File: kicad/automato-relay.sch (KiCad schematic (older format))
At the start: 30 parts, among them J1 Screw_Terminal_01x03, J2 Screw_Terminal_01x03, J3 Screw_Terminal_01x03, J4 Screw_Terminal_01x05, J5 Screw_Terminal_01x03, J6 Screw_Terminal_01x03, J7 Screw_Terminal_01x05, J8 Screw_Terminal_01x03, K1 G5LE-14, K2 G5LE-14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

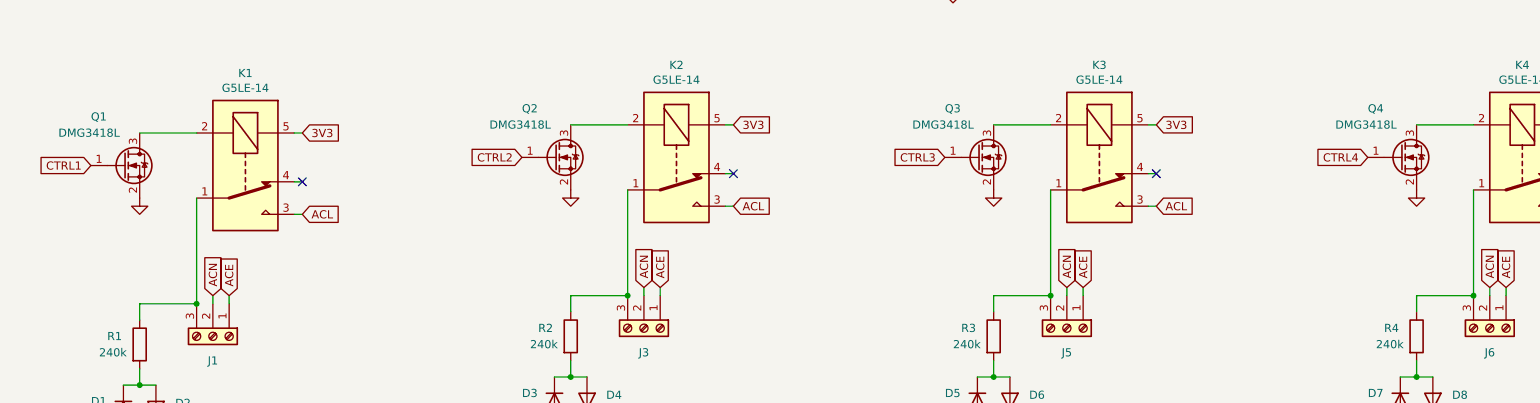
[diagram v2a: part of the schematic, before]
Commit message: add pull-down resistors to MOSFET gates
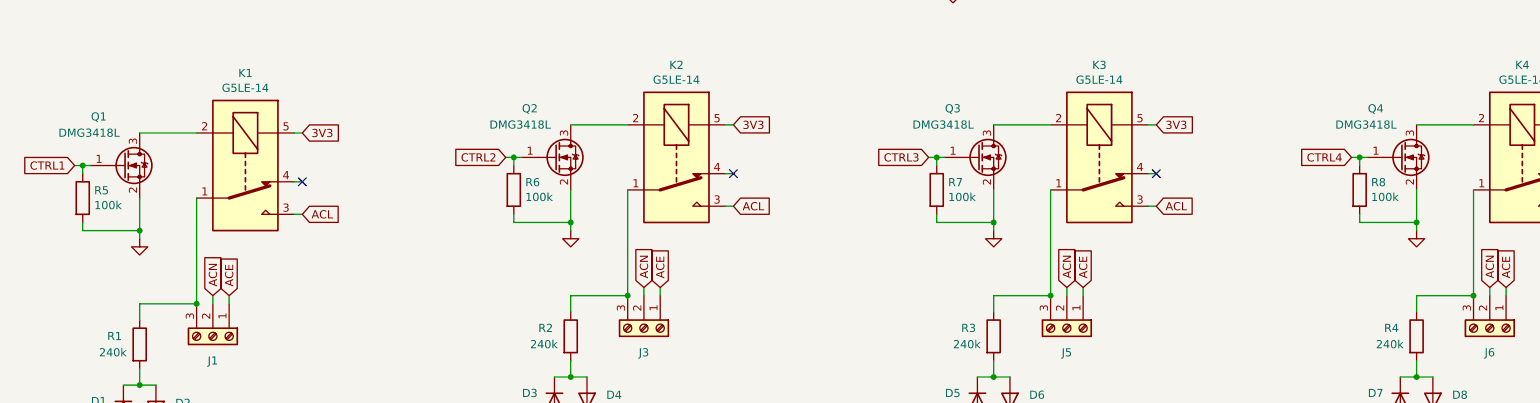
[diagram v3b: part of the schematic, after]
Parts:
- added R5, R6, R7, R8: 100k, symbol Device:R
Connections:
- net CTRL1: now also R5.1
- net CTRL2: now also R6.1
- net CTRL3: now also R7.1
- net CTRL4: now also R8.1
- net GND: now also R5.2, R6.2, R7.2, R8.2
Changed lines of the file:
@@
 L power:GND #PWR02
 U 1 1 60165E6B
-P 1600 4400
-F 0 "#PWR02" H 1600 4150 50  0001 C CNN
-F 1 "GND" H 1450 4350 50  0001 C CNN
-F 2 "" H 1600 4400 50  0001 C CNN
-F 3 "" H 1600 4400 50  0001 C CNN
-	1    1600 4400
+P 1600 4650
+F 0 "#PWR02" H 1600 4400 50  0001 C CNN
+F 1 "GND" H 1450 4600 50  0001 C CNN
+F 2 "" H 1600 4650 50  0001 C CNN
+F 3 "" H 1600 4650 50  0001 C CNN
+	1    1600 4650
 	1    0    0    -1
 $EndComp
@@
 Text GLabel 2600 4500 2    50   Input ~ 0
 ACL
-Text GLabel 1300 4200 0    50   Input ~ 0
+Text GLabel 1200 4200 0    50   Input ~ 0
 CTRL1
 Wire Wire Line
@@
 Text GLabel 5250 4450 2    50   Input ~ 0
 ACL
-Text GLabel 3950 4150 0    50   Input ~ 0
+Text GLabel 3850 4150 0    50   Input ~ 0
 CTRL2
 Wire Wire Line
@@
 Text GLabel 7850 4450 2    50   Input ~ 0
 ACL
-Text GLabel 6550 4150 0    50   Input ~ 0
+Text GLabel 6450 4150 0    50   Input ~ 0
 CTRL3
 Wire Wire Line
@@
 Text GLabel 10450 4450 2    50   Input ~ 0
 ACL
-Text GLabel 9150 4150 0    50   Input ~ 0
+Text GLabel 9050 4150 0    50   Input ~ 0
 CTRL4
 Wire Wire Line
@@
 Text GLabel 9450 5900 3    50   Input ~ 0
 ACN
-$Comp
-L Transistor_FET:DMG3418L Q1
-U 1 1 6025169E
-P 1500 4200
-F 0 "Q1" H 1300 4500 50  0000 L CNN
-F 1 "DMG3418L" H 1100 4400 50  0000 L CNN
-F 2 "Package_TO_SOT_SMD:SOT-23" H 1700 4125 50  0001 L CIN
-F 3 "http://www.diodes.com/assets/Datasheets/DMG3418L.pdf" H 1500 4200 50  0001 L CNN
-	1    1500 4200
-	1    0    0    -1
-$EndComp
 Wire Wire Line
 	1600 4000 1950 4000
 Text GLabel 2600 4000 2    50   Input ~ 0
 3V3
-$Comp
-L power:GND #PWR01
-U 1 1 6025E6F9
-P 4250 4350
-F 0 "#PWR01" H 4250 4100 50  0001 C CNN
-F 1 "GND" H 4100 4300 50  0001 C CNN
-F 2 "" H 4250 4350 50  0001 C CNN
-F 3 "" H 4250 4350 50  0001 C CNN
-	1    4250 4350
-	1    0    0    -1
-$EndComp
 $Comp
 L Transistor_FET:DMG3418L Q2
@@
 	4250 3950 4600 3950
 $Comp
-L power:GND #PWR03
-U 1 1 6026325E
-P 6850 4350
-F 0 "#PWR03" H 6850 4100 50  0001 C CNN
-F 1 "GND" H 6700 4300 50  0001 C CNN
-F 2 "" H 6850 4350 50  0001 C CNN
-F 3 "" H 6850 4350 50  0001 C CNN
-	1    6850 4350
-	1    0    0    -1
-$EndComp
-$Comp
 L Transistor_FET:DMG3418L Q3
 U 1 1 60263271
@@
 Wire Wire Line
 	6850 3950 7200 3950
-$Comp
-L power:GND #PWR04
-U 1 1 602684FF
-P 9450 4350
-F 0 "#PWR04" H 9450 4100 50  0001 C CNN
-F 1 "GND" H 9300 4300 50  0001 C CNN
-F 2 "" H 9450 4350 50  0001 C CNN
-F 3 "" H 9450 4350 50  0001 C CNN
-	1    9450 4350
-	1    0    0    -1
-$EndComp
 $Comp
 L Transistor_FET:DMG3418L Q4
@@
 Wire Wire Line
 	4800 4950 4800 5000
+$Comp
+L Device:R R5
+U 1 1 6030A4D9
+P 1250 4400
+F 0 "R5" H 1320 4446 50  0000 L CNN
+F 1 "100k" H 1320 4355 50  0000 L CNN
+F 2 "" V 1180 4400 50  0001 C CNN
+F 3 "~" H 1250 4400 50  0001 C CNN
+	1    1250 4400
+	1    0    0    -1
+$EndComp
+Wire Wire Line
+	1200 4200 1250 4200
+Wire Wire Line
+	1250 4200 1250 4250
+Connection ~ 1250 4200
+Wire Wire Line
+	1250 4200 1300 4200
+Wire Wire Line
+	1250 4550 1250 4600
+Wire Wire Line
+	1250 4600 1600 4600
+Wire Wire Line
+	1600 4400 1600 4600
+Connection ~ 1600 4600
+$Comp
+L power:GND #PWR01
+U 1 1 6031750C
+P 4250 4600
+F 0 "#PWR01" H 4250 4350 50  0001 C CNN
+F 1 "GND" H 4100 4550 50  0001 C CNN
+F 2 "" H 4250 4600 50  0001 C CNN
+F 3 "" H 4250 4600 50  0001 C CNN
+	1    4250 4600
+	1    0    0    -1
+$EndComp
+$Comp
+L Device:R R6
+U 1 1 6031751E
+P 3900 4350
+F 0 "R6" H 3970 4396 50  0000 L CNN
+F 1 "100k" H 3970 4305 50  0000 L CNN
+F 2 "" V 3830 4350 50  0001 C CNN
+F 3 "~" H 3900 4350 50  0001 C CNN
+	1    3900 4350
+	1    0    0    -1
+$EndComp
+Wire Wire Line
+	3900 4500 3900 4550
+Wire Wire Line
+	3900 4550 4250 4550
+Wire Wire Line
+	4250 4350 4250 4550
+Connection ~ 4250 4550
+Wire Wire Line
+	3850 4150 3900 4150
+Wire Wire Line
+	3900 4150 3900 4200
+Connection ~ 3900 4150
+Wire Wire Line
+	3900 4150 3950 4150
+$Comp
+L Transistor_FET:DMG3418L Q1
+U 1 1 6025169E
+P 1500 4200
+F 0 "Q1" H 1300 4500 50  0000 L CNN
+F 1 "DMG3418L" H 1100 4400 50  0000 L CNN
+F 2 "Package_TO_SOT_SMD:SOT-23" H 1700 4125 50  0001 L CIN
+F 3 "http://www.diodes.com/assets/Datasheets/DMG3418L.pdf" H 1500 4200 50  0001 L CNN
+	1    1500 4200
+	1    0    0    -1
+$EndComp
+Wire Wire Line
+	4250 4550 4250 4600
+Wire Wire Line
+	1600 4600 1600 4650
+$Comp
+L power:GND #PWR03
+U 1 1 60330C2B
+P 6850 4600
+F 0 "#PWR03" H 6850 4350 50  0001 C CNN
+F 1 "GND" H 6700 4550 50  0001 C CNN
+F 2 "" H 6850 4600 50  0001 C CNN
+F 3 "" H 6850 4600 50  0001 C CNN
+	1    6850 4600
+	1    0    0    -1
+$EndComp
+$Comp
+L Device:R R7
+U 1 1 60330C3D
+P 6500 4350
+F 0 "R7" H 6570 4396 50  0000 L CNN
+F 1 "100k" H 6570 4305 50  0000 L CNN
+F 2 "" V 6430 4350 50  0001 C CNN
+F 3 "~" H 6500 4350 50  0001 C CNN
+	1    6500 4350
+	1    0    0    -1
+$EndComp
+Wire Wire Line
+	6500 4500 6500 4550
+Wire Wire Line
+	6500 4550 6850 4550
+Wire Wire Line
+	6850 4350 6850 4550
+Connection ~ 6850 4550
+Wire Wire Line
+	6850 4550 6850 4600
+Wire Wire Line
+	6450 4150 6500 4150
+Wire Wire Line
+	6500 4150 6500 4200
+Connection ~ 6500 4150
+Wire Wire Line
+	6500 4150 6550 4150
+$Comp
+L power:GND #PWR04
+U 1 1 6033C766
+P 9450 4600
+F 0 "#PWR04" H 9450 4350 50  0001 C CNN
+F 1 "GND" H 9300 4550 50  0001 C CNN
+F 2 "" H 9450 4600 50  0001 C CNN
+F 3 "" H 9450 4600 50  0001 C CNN
+	1    9450 4600
+	1    0    0    -1
+$EndComp
+$Comp
+L Device:R R8
+U 1 1 6033C778
+P 9100 4350
+F 0 "R8" H 9170 4396 50  0000 L CNN
+F 1 "100k" H 9170 4305 50  0000 L CNN
+F 2 "" V 9030 4350 50  0001 C CNN
+F 3 "~" H 9100 4350 50  0001 C CNN
+	1    9100 4350
+	1    0    0    -1
+$EndComp
+Wire Wire Line
+	9100 4500 9100 4550
+Wire Wire Line
+	9100 4550 9450 4550
+Wire Wire Line
+	9450 4350 9450 4550
+Connection ~ 9450 4550
+Wire Wire Line
+	9450 4550 9450 4600
+Wire Wire Line
+	9150 4150 9100 4150
+Wire Wire Line
+	9100 4150 9100 4200
+Connection ~ 9100 4150
+Wire Wire Line
+	9100 4150 9050 4150
 $EndSCHEMATC

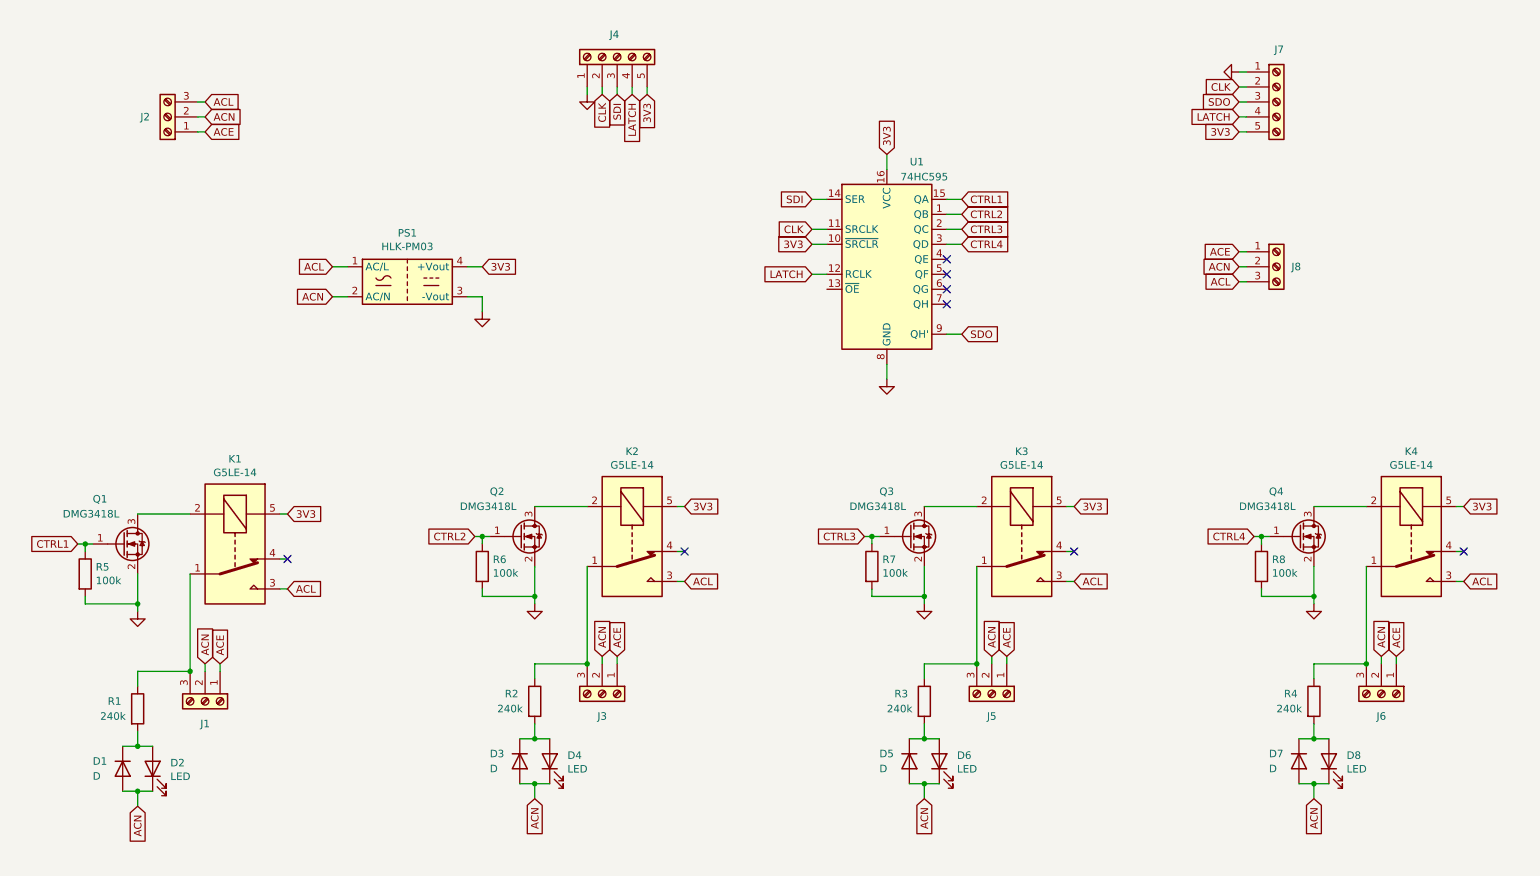
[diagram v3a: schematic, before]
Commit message: add TE-3-213598-4 symbol
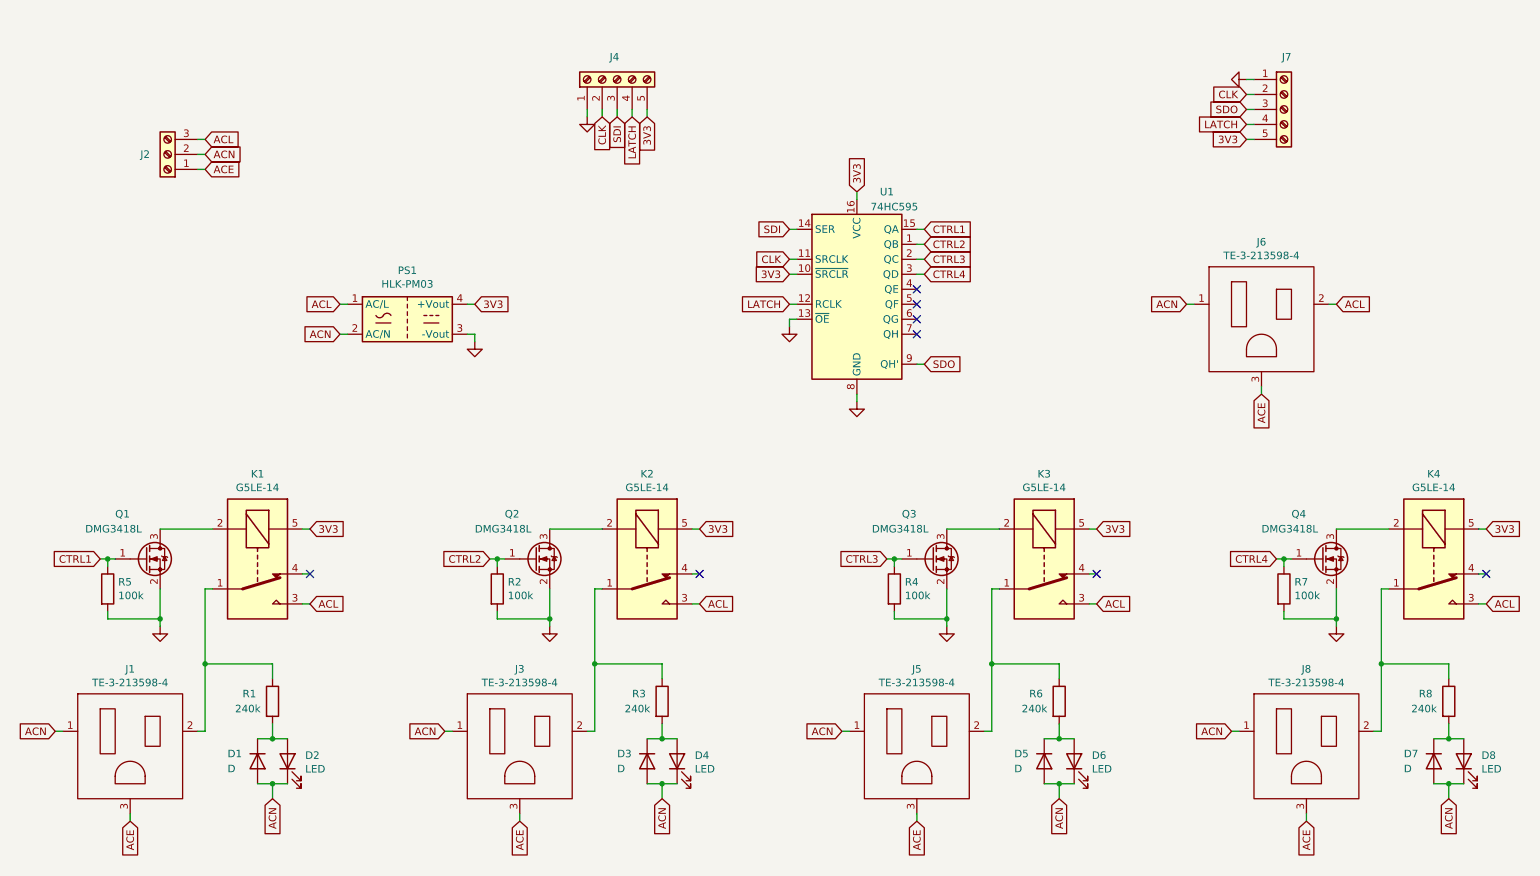
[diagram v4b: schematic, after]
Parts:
- removed J1, J3, J5, J6, J8: Screw_Terminal_01x03, symbol Connector:Screw_Terminal_01x03
- added J1, J3, J5, J6, J8: TE-3-213598-4, symbol automato-relay:TE-3-213598-4
- R2, R4: value 240k -> 100k
- R6, R8: value 100k -> 240k
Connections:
- net ACE: now also J1.3 (Earth), J3.3 (Earth), J5.3 (Earth), J6.3 (Earth), J8.3 (Earth)
- net ACL: now also J6.2 (Hot)
- net ACN: now also J1.1 (Neutral), J3.1 (Neutral), J5.1 (Neutral), J6.1 (Neutral), J8.1 (Neutral)
- net CTRL2: now also R2.1; no longer R6.1
- net CTRL3: now also R4.1; no longer R7.1
- net CTRL4: now also R7.1; no longer R8.1
- net GND: now also R2.2, R4.2, U1.13 (~OE); no longer R6.2, R8.2
- net at K1.1, R1.1: now also J1.2 (Hot)
- net at K2.1: now also R3.1, J3.2 (Hot); no longer R2.1
- net at K3.1: now also R6.1, J5.2 (Hot); no longer R3.1
- net at K4.1: now also R8.1, J8.2 (Hot); no longer R4.1
- net at D3.1 (K), D4.2 (A): now also R3.2; no longer R2.2
- net at D5.1 (K), D6.2 (A): now also R6.2; no longer R3.2
- net at D7.1 (K), D8.2 (A): now also R8.2; no longer R4.2
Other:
- moved on the sheet: D1, D2, J2, J4, J7, K1, PS1, Q1, R1, R5, U1
